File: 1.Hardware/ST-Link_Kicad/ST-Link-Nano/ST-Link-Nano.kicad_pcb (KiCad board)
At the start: 2 copper layers, 29.2 x 12.7 mm, 26 parts, among them J1 Type-C, J2 JUMP, J3 Conn_02x04_Top_Bottom, U1 XC6210B332MR, U2 STM32F103CBTx, Y1 Crystal_GND24_Small

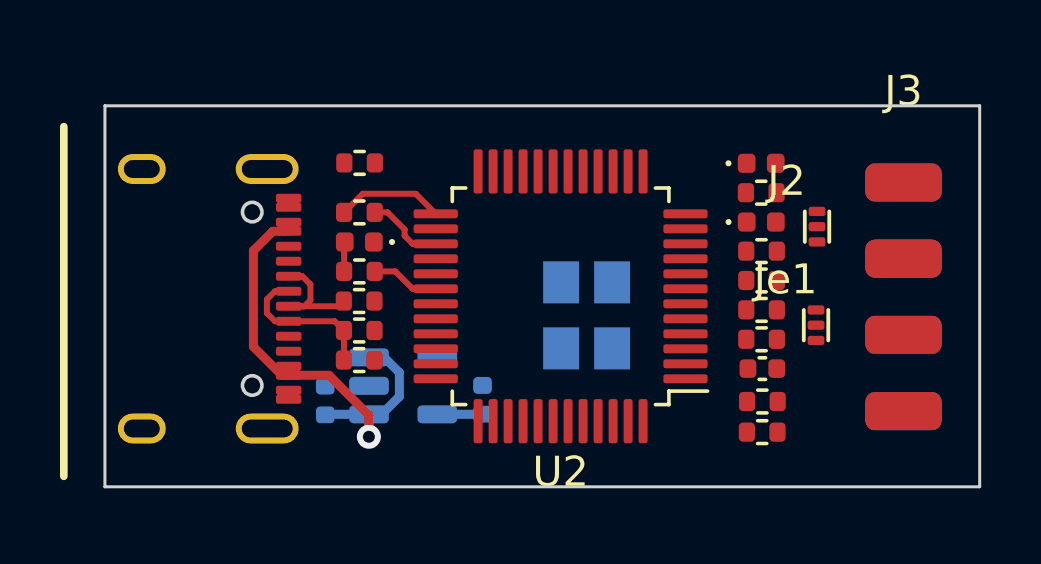
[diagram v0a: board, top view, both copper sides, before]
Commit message: 已完成PCB，输出Gerber文件
2022/8/7
今天把之前剩下一半的PCB画完了，输出了Gerber，准备到嘉立创打样，然后在淘宝上买器件回来自己焊接。
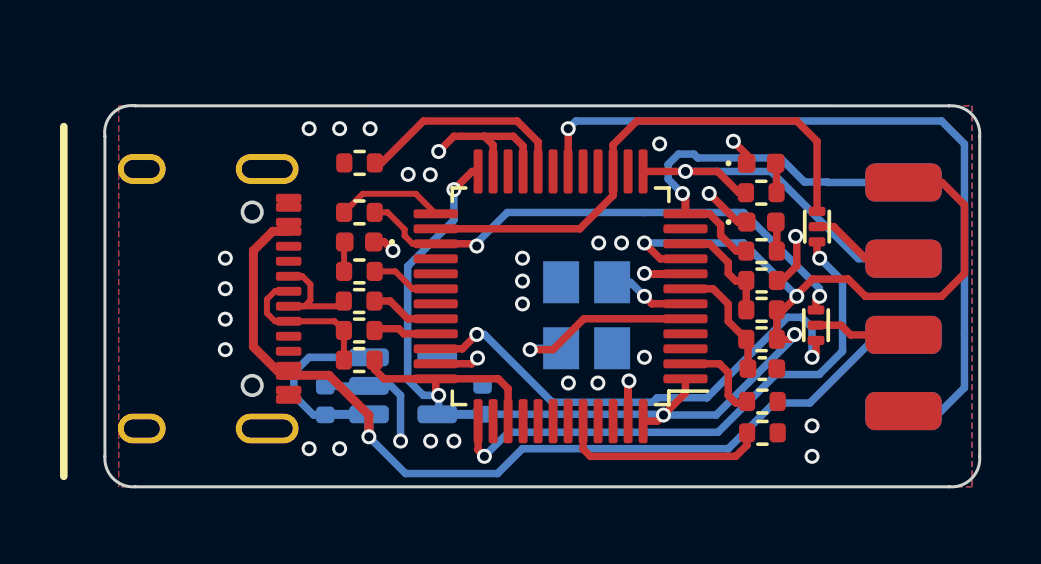
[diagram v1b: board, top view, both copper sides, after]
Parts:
- turned R4 to 0 degrees
- turned R5 to 180 degrees
- turned R7 to 180 degrees
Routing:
- net +3V3: track 1.51 -> 53.0 mm, vias 0 -> 6
- net /nRST: track 0.00 -> 25.5 mm, vias 0 -> 1
- net +5V: track 15.7 -> 38.0 mm
- net GND: track 0.00 -> 20.9 mm, vias 0 -> 33
- net /ST_SWCLK: track 0.00 -> 18.6 mm, vias 0 -> 2
- net /JTCK: track 0.00 -> 17.8 mm
- net /ST_SWDIO: track 0.00 -> 16.6 mm, vias 0 -> 2
- net /JTMS: track 2.59 -> 17.5 mm, vias 0 -> 2
- net /TX: track 0.00 -> 13.4 mm, vias 0 -> 1
- net /RX: track 0.00 -> 12.2 mm, vias 0 -> 1
- net Net-(R6-Pad1): track 0.00 -> 7.29 mm
- net Net-(R2-Pad1): track 0.00 -> 7.08 mm
- net Net-(U2-Pad5): track 0.00 -> 6.66 mm, vias 0 -> 1
- net Net-(C1-Pad1): track 0.00 -> 4.06 mm
- net Net-(R4-Pad1): track 0.00 -> 3.74 mm
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- added copper zone on B.Cu, net GND
- added copper zone on F.Cu, net GND
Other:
- outline, holes or cut-outs redrawn
